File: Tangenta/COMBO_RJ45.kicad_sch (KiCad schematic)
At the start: 1 part, among them J14 RC01133

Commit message: RS-485/422 revisited.
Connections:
- net RS_CONN_GND: now reaches J14.9
- no-connect marks 6 -> 5
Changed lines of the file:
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@@
   (no_connect (at 136.525 73.025))
   (no_connect (at 151.765 93.345))
-  (no_connect (at 151.765 65.405))
   (no_connect (at 136.525 78.105))
   (bus_entry (at 50.8 31.115) (size 2.54 -2.54)
@@
     (stroke (width 0) (type default))
   )
+  (wire (pts (xy 151.765 65.405) (xy 151.765 62.865))
+    (stroke (width 0) (type default))
+  )
   (wire (pts (xy 53.34 28.575) (xy 71.755 28.575))
     (stroke (width 0) (type default))
@@
     (stroke (width 0) (type default))
   )
+  (wire (pts (xy 120.65 62.865) (xy 151.765 62.865))
+    (stroke (width 0) (type default))
+  )
   (bus (pts (xy 50.8 36.195) (xy 50.8 38.735))
+    (stroke (width 0) (type default))
+  )
+  (wire (pts (xy 46.99 49.53) (xy 71.755 49.53))
     (stroke (width 0) (type default))
   )
@@
     (stroke (width 0) (type default))
   )
+  (label "RS_GND" (at 120.65 62.865 0) (fields_autoplaced)
+    (effects (font (size 1.27 1.27)) (justify left bottom))
+  )
   (label "RS.R_N" (at 120.65 80.645 0) (fields_autoplaced)
     (effects (font (size 1.27 1.27)) (justify left bottom))
@@
     (effects (font (size 1.27 1.27)) (justify left bottom))
   )
+  (label "RS_GND" (at 71.755 49.53 180) (fields_autoplaced)
+    (effects (font (size 1.27 1.27)) (justify right bottom))
+  )
   (label "RS.D_P" (at 120.65 85.725 0) (fields_autoplaced)
     (effects (font (size 1.27 1.27)) (justify left bottom))
@@
     (effects (font (size 1.27 1.27)) (justify right))
   )
+  (hierarchical_label "RS_CONN_GND" (shape bidirectional) (at 46.99 49.53 180) (fields_autoplaced)
+    (effects (font (size 1.27 1.27)) (justify right))
+  )

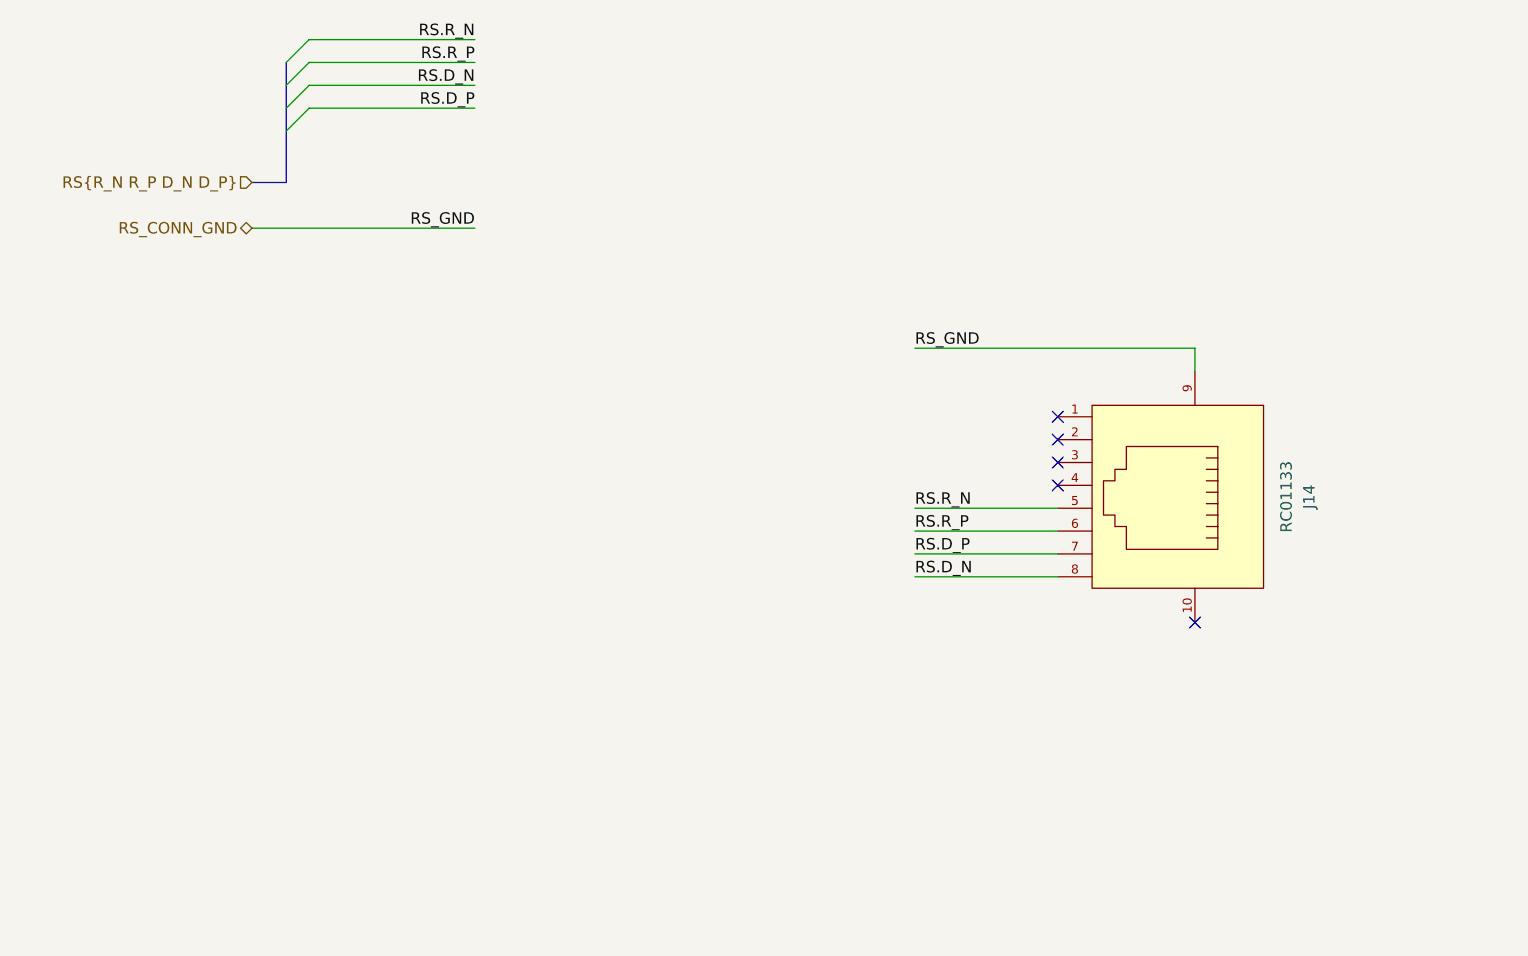
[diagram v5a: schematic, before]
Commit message: CANbus done, UART terminals in progress...
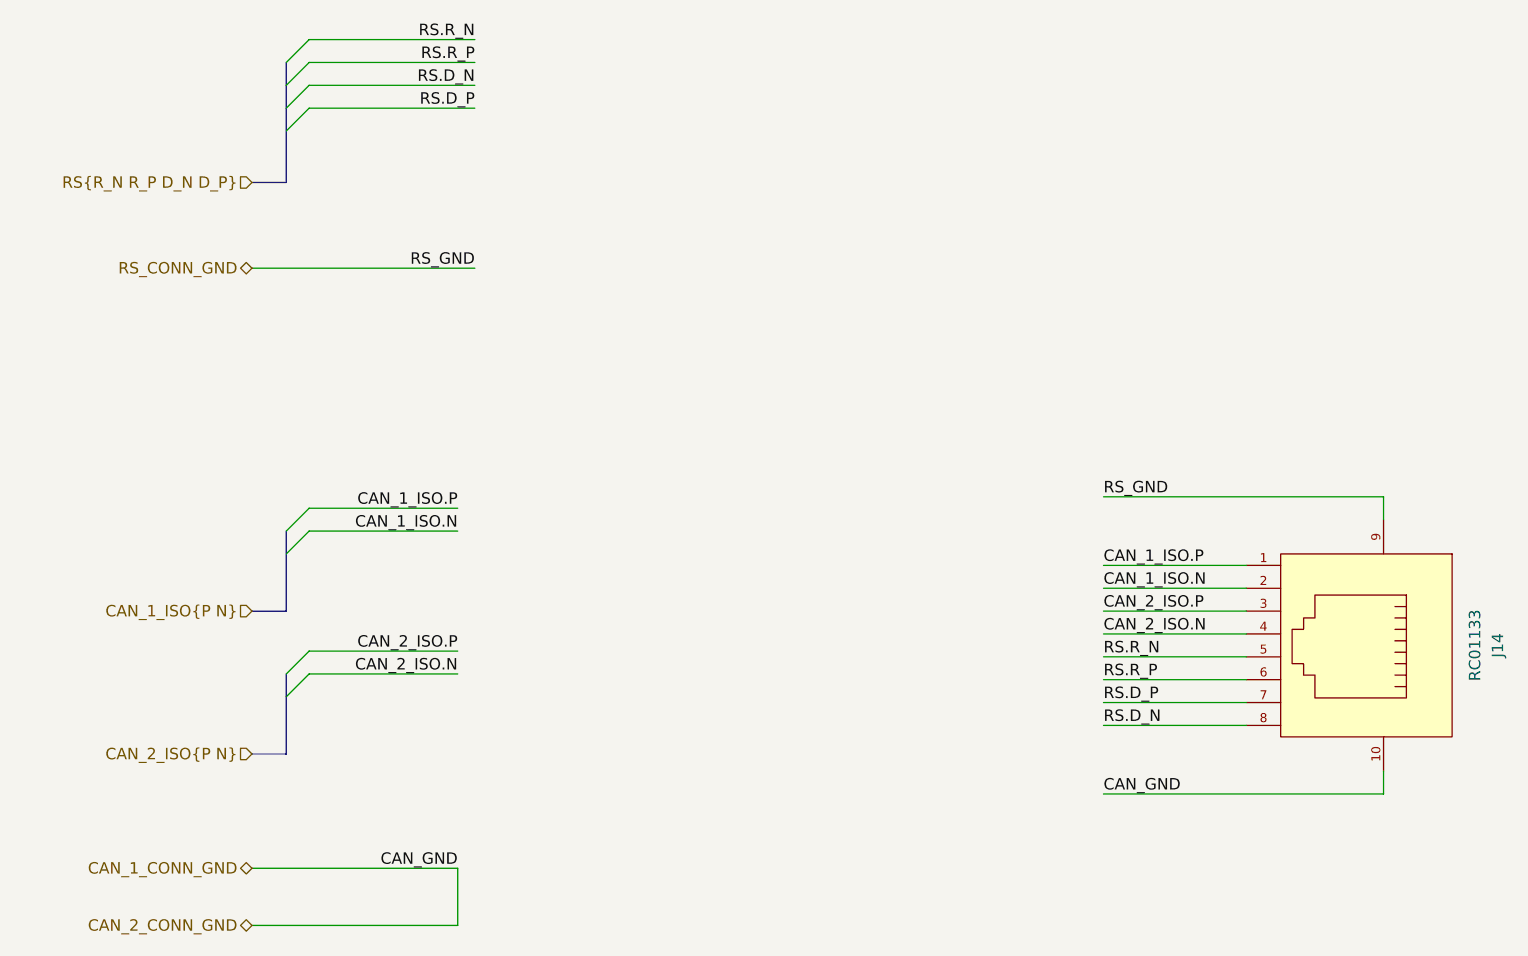
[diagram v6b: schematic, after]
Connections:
- net CAN_1_ISO.P: now reaches J14.1
- net CAN_1_CONN_GND: now reaches J14.10
- net CAN_1_ISO.N: now reaches J14.2
- net CAN_2_ISO.P: now reaches J14.3
- net CAN_2_ISO.N: now reaches J14.4
- no-connect marks 5 -> 0
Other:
- moved on the sheet: J14
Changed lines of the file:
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@@
 (kicad_sch (version 20230121) (generator eeschema)
   (paper "A4")
-  (no_connect (at 136.525 75.565))
-  (no_connect (at 136.525 70.485))
-  (no_connect (at 136.525 73.025))
-  (no_connect (at 151.765 93.345))
-  (no_connect (at 136.525 78.105))
+  (bus_entry (at 50.8 99.06) (size 2.54 -2.54)
+    (stroke (width 0) (type default))
+  )
   (bus_entry (at 50.8 31.115) (size 2.54 -2.54)
     (stroke (width 0) (type default))
   )
+  (bus_entry (at 50.8 101.6) (size 2.54 -2.54)
+    (stroke (width 0) (type default))
+  )
+  (bus_entry (at 50.8 83.185) (size 2.54 -2.54)
+    (stroke (width 0) (type default))
+  )
+  (bus_entry (at 50.8 85.725) (size 2.54 -2.54)
+    (stroke (width 0) (type default))
+  )
   (bus_entry (at 50.8 33.655) (size 2.54 -2.54)
     (stroke (width 0) (type default))
@@
     (stroke (width 0) (type default))
   )
+  (wire (pts (xy 157.48 92.075) (xy 141.605 92.075))
+    (stroke (width 0) (type default))
+  )
+  (wire (pts (xy 69.85 120.65) (xy 69.85 127))
+    (stroke (width 0) (type default))
+  )
   (wire (pts (xy 53.34 36.195) (xy 71.755 36.195))
     (stroke (width 0) (type default))
   )
-  (wire (pts (xy 151.765 65.405) (xy 151.765 62.865))
+  (wire (pts (xy 172.72 81.915) (xy 172.72 79.375))
     (stroke (width 0) (type default))
   )
@@
     (stroke (width 0) (type default))
   )
-  (wire (pts (xy 120.65 62.865) (xy 151.765 62.865))
+  (wire (pts (xy 141.605 79.375) (xy 172.72 79.375))
     (stroke (width 0) (type default))
   )
@@
     (stroke (width 0) (type default))
   )
-  (wire (pts (xy 46.99 49.53) (xy 71.755 49.53))
-    (stroke (width 0) (type default))
-  )
-  (wire (pts (xy 136.525 85.725) (xy 120.65 85.725))
+  (bus (pts (xy 46.99 92.075) (xy 50.8 92.075))
+    (stroke (width 0) (type default))
+  )
+  (wire (pts (xy 53.34 99.06) (xy 69.85 99.06))
+    (stroke (width 0) (type default))
+  )
+  (bus (pts (xy 50.8 101.6) (xy 50.8 107.95))
+    (stroke (width 0) (type default))
+  )
+  (wire (pts (xy 46.99 53.975) (xy 71.755 53.975))
+    (stroke (width 0) (type default))
+  )
+  (wire (pts (xy 46.99 127) (xy 69.85 127))
+    (stroke (width 0) (type default))
+  )
+  (wire (pts (xy 157.48 102.235) (xy 141.605 102.235))
+    (stroke (width 0) (type default))
+  )
+  (wire (pts (xy 53.34 83.185) (xy 69.85 83.185))
+    (stroke (width 0) (type default))
+  )
+  (wire (pts (xy 46.99 120.65) (xy 69.85 120.65))
+    (stroke (width 0) (type default))
+  )
+  (wire (pts (xy 141.605 112.395) (xy 172.72 112.395))
+    (stroke (width 0) (type default))
+  )
+  (bus (pts (xy 46.99 107.95) (xy 50.8 107.95))
+    (stroke (width 0) (type default))
+  )
+  (bus (pts (xy 50.8 99.06) (xy 50.8 101.6))
     (stroke (width 0) (type default))
   )
@@
     (stroke (width 0) (type default))
   )
-  (wire (pts (xy 136.525 88.265) (xy 120.65 88.265))
+  (wire (pts (xy 157.48 104.775) (xy 141.605 104.775))
+    (stroke (width 0) (type default))
+  )
+  (wire (pts (xy 157.48 86.995) (xy 141.605 86.995))
     (stroke (width 0) (type default))
   )
@@
     (stroke (width 0) (type default))
   )
+  (wire (pts (xy 53.34 96.52) (xy 69.85 96.52))
+    (stroke (width 0) (type default))
+  )
+  (bus (pts (xy 50.8 83.185) (xy 50.8 85.725))
+    (stroke (width 0) (type default))
+  )
+  (wire (pts (xy 157.48 89.535) (xy 141.605 89.535))
+    (stroke (width 0) (type default))
+  )
+  (wire (pts (xy 157.48 94.615) (xy 141.605 94.615))
+    (stroke (width 0) (type default))
+  )
   (bus (pts (xy 50.8 38.735) (xy 50.8 44.45))
     (stroke (width 0) (type default))
   )
-  (wire (pts (xy 136.525 83.185) (xy 120.65 83.185))
+  (wire (pts (xy 53.34 80.645) (xy 69.85 80.645))
+    (stroke (width 0) (type default))
+  )
+  (bus (pts (xy 50.8 85.725) (xy 50.8 92.075))
+    (stroke (width 0) (type default))
+  )
+  (wire (pts (xy 157.48 99.695) (xy 141.605 99.695))
     (stroke (width 0) (type default))
   )
@@
     (stroke (width 0) (type default))
   )
-  (wire (pts (xy 136.525 80.645) (xy 120.65 80.645))
-    (stroke (width 0) (type default))
-  )
-  (label "RS_GND" (at 120.65 62.865 0) (fields_autoplaced)
-    (effects (font (size 1.27 1.27)) (justify left bottom))
-  )
-  (label "RS.R_N" (at 120.65 80.645 0) (fields_autoplaced)
+  (wire (pts (xy 172.72 109.855) (xy 172.72 112.395))
+    (stroke (width 0) (type default))
+  )
+  (wire (pts (xy 157.48 97.155) (xy 141.605 97.155))
+    (stroke (width 0) (type default))
+  )
+  (label "RS_GND" (at 141.605 79.375 0) (fields_autoplaced)
+    (effects (font (size 1.27 1.27)) (justify left bottom))
+  )
+  (label "RS.R_N" (at 141.605 97.155 0) (fields_autoplaced)
     (effects (font (size 1.27 1.27)) (justify left bottom))
   )
@@
     (effects (font (size 1.27 1.27)) (justify right bottom))
   )
+  (label "CAN_2_ISO.N" (at 69.85 99.06 180) (fields_autoplaced)
+    (effects (font (size 1.27 1.27)) (justify right bottom))
+  )
+  (label "CAN_1_ISO.P" (at 69.85 80.645 180) (fields_autoplaced)
+    (effects (font (size 1.27 1.27)) (justify right bottom))
+  )
+  (label "CAN_GND" (at 141.605 112.395 0) (fields_autoplaced)
+    (effects (font (size 1.27 1.27)) (justify left bottom))
+  )
   (label "RS.D_P" (at 71.755 36.195 180) (fields_autoplaced)
     (effects (font (size 1.27 1.27)) (justify right bottom))
   )
+  (label "CAN_2_ISO.P" (at 141.605 92.075 0) (fields_autoplaced)
+    (effects (font (size 1.27 1.27)) (justify left bottom))
+  )
   (label "RS.R_N" (at 71.755 28.575 180) (fields_autoplaced)
     (effects (font (size 1.27 1.27)) (justify right bottom))
   )
-  (label "RS.R_P" (at 120.65 83.185 0) (fields_autoplaced)
-    (effects (font (size 1.27 1.27)) (justify left bottom))
-  )
-  (label "RS.D_N" (at 120.65 88.265 0) (fields_autoplaced)
-    (effects (font (size 1.27 1.27)) (justify left bottom))
-  )
-  (label "RS_GND" (at 71.755 49.53 180) (fields_autoplaced)
-    (effects (font (size 1.27 1.27)) (justify right bottom))
-  )
-  (label "RS.D_P" (at 120.65 85.725 0) (fields_autoplaced)
-    (effects (font (size 1.27 1.27)) (justify left bottom))
+  (label "RS.R_P" (at 141.605 99.695 0) (fields_autoplaced)
+    (effects (font (size 1.27 1.27)) (justify left bottom))
+  )
+  (label "RS.D_N" (at 141.605 104.775 0) (fields_autoplaced)
+    (effects (font (size 1.27 1.27)) (justify left bottom))
+  )
+  (label "CAN_2_ISO.N" (at 141.605 94.615 0) (fields_autoplaced)
+    (effects (font (size 1.27 1.27)) (justify left bottom))
+  )
+  (label "CAN_2_ISO.P" (at 69.85 96.52 180) (fields_autoplaced)
+    (effects (font (size 1.27 1.27)) (justify right bottom))
+  )
+  (label "RS_GND" (at 71.755 53.975 180) (fields_autoplaced)
+    (effects (font (size 1.27 1.27)) (justify right bottom))
+  )
+  (label "CAN_1_ISO.P" (at 141.605 86.995 0) (fields_autoplaced)
+    (effects (font (size 1.27 1.27)) (justify left bottom))
+  )
+  (label "CAN_GND" (at 69.85 120.65 180) (fields_autoplaced)
+    (effects (font (size 1.27 1.27)) (justify right bottom))
+  )
+  (label "RS.D_P" (at 141.605 102.235 0) (fields_autoplaced)
+    (effects (font (size 1.27 1.27)) (justify left bottom))
+  )
+  (label "CAN_1_ISO.N" (at 69.85 83.185 180) (fields_autoplaced)
+    (effects (font (size 1.27 1.27)) (justify right bottom))
+  )
+  (label "CAN_1_ISO.N" (at 141.605 89.535 0) (fields_autoplaced)
+    (effects (font (size 1.27 1.27)) (justify left bottom))
+  )
+  (hierarchical_label "CAN_2_ISO{P N}" (shape input) (at 46.99 107.95 180) (fields_autoplaced)
+    (effects (font (size 1.27 1.27)) (justify right))
+  )
+  (hierarchical_label "CAN_1_ISO{P N}" (shape input) (at 46.99 92.075 180) (fields_autoplaced)
+    (effects (font (size 1.27 1.27)) (justify right))
   )
   (hierarchical_label "RS{R_N R_P D_N D_P}" (shape input) (at 46.99 44.45 180) (fields_autoplaced)
     (effects (font (size 1.27 1.27)) (justify right))
   )
-  (hierarchical_label "RS_CONN_GND" (shape bidirectional) (at 46.99 49.53 180) (fields_autoplaced)
-    (effects (font (size 1.27 1.27)) (justify right))
-  )
-  (symbol (lib_id "RJ45_SIMPLE:RC01133") (at 146.685 80.645 270) (unit 1)
+  (hierarchical_label "CAN_1_CONN_GND" (shape bidirectional) (at 46.99 120.65 180) (fields_autoplaced)
+    (effects (font (size 1.27 1.27)) (justify right))
+  )
+  (hierarchical_label "CAN_2_CONN_GND" (shape bidirectional) (at 46.99 127 180) (fields_autoplaced)
+    (effects (font (size 1.27 1.27)) (justify right))
+  )
+  (hierarchical_label "RS_CONN_GND" (shape bidirectional) (at 46.99 53.975 180) (fields_autoplaced)
+    (effects (font (size 1.27 1.27)) (justify right))
+  )
+  (symbol (lib_id "RJ45_SIMPLE:RC01133") (at 167.64 97.155 270) (unit 1)
     (in_bom yes) (on_board yes) (dnp no) (fields_autoplaced)
-    (property "Reference" "J14" (at 164.465 79.375 0)
+    (property "Reference" "J14" (at 185.42 95.885 0)
       (effects (font (size 1.27 1.27)))
     )
-    (property "Value" "RC01133" (at 161.925 79.375 0)
+    (property "Value" "RC01133" (at 182.88 95.885 0)
       (effects (font (size 1.27 1.27)))
     )
-    (property "Footprint" "RJ45_SIMPLE:RJ45_SIMPLE" (at 121.285 81.915 0)
+    (property "Footprint" "RJ45_SIMPLE:RJ45_SIMPLE" (at 142.24 98.425 0)
       (effects (font (size 1.27 1.27) italic) hide)
     )
-    (property "Datasheet" "https://atta.szlcsc.com/upload/public/pdf/source/20200728/C708616_F79F0C1A8A5D9701E7B7144C9F29FA5C.pdf" (at 118.745 69.215 0)
+    (property "Datasheet" "https://atta.szlcsc.com/upload/public/pdf/source/20200728/C708616_F79F0C1A8A5D9701E7B7144C9F29FA5C.pdf" (at 139.7 85.725 0)
       (effects (font (size 1.27 1.27)) (justify left) hide)
     )
-    (property "LCSC" "C708616" (at 123.825 74.295 0)
+    (property "LCSC" "C708616" (at 144.78 90.805 0)
       (effects (font (size 1.27 1.27)) hide)
     )

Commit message: Libraries exported from global to project.
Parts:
- J14: symbol RJ45_SIMPLE:RC01133 -> CholaSymbolsPrjLib:RC01133
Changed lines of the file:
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@@
     (effects (font (size 1.27 1.27)) (justify right))
   )
-  (symbol (lib_id "RJ45_SIMPLE:RC01133") (at 167.64 97.155 270) (unit 1)
+  (symbol (lib_id "CholaSymbolsPrjLib:RC01133") (at 167.64 97.155 270) (unit 1)
     (in_bom yes) (on_board yes) (dnp no) (fields_autoplaced)
     (property "Reference" "J14" (at 185.42 95.885 0)
